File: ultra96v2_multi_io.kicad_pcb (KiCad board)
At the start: 2 copper layers, 85 x 54 mm, 85 parts, among them J1 TE 5179030-2, J2 57202-G52-20LF, J3 1-1734248-5, J4 1-1734248-5, J5 PMOD, J6 PMOD, J7 PinHeader, J8 Conn_01x04, Q1 DMN63D8LDW-7, Q2 DMN63D8LDW-7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

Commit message: rev2
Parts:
- J3, J4: footprint myfootprint:55510-140LF -> myfootprint:55510-140LF_handsolder
- L2: value 2.2uH MLZ2012A2R2MT -> 2.2uH 2012
- U1: value LM3671MF-3.3/NOPB -> LM3671MF-3.3
- moved R22 4.21 mm to (150.9, 129.7)
- moved C12 2.19 mm to (150.7, 134.5)
- moved C11 1.61 mm to (129.4, 133.0), turned to 180 degrees
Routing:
- net GND: track 554.3 -> 637.2 mm, vias 71 -> 88
- net /CAM1_SCL: track 41.7 -> 50.8 mm
- net /CAM1_CLK: track 44.0 -> 53.1 mm
- net /CAM1_SDA: track 44.3 -> 51.9 mm
- net /CAM1_GPIO: track 44.8 -> 52.4 mm, vias 1 -> 2
- net +3V3: track 172.9 -> 179.9 mm
- net /HS_CSI0_CLK_P: track 16.8 -> 10.3 mm
- net /HS_CSI0_D0_N: track 16.8 -> 22.3 mm
- net /CAM0_GPIO: track 17.0 -> 21.6 mm
- net /HS_SPI1_SCLK: track 14.5 -> 18.6 mm
- net /CAM0_CLK: track 14.6 -> 18.6 mm
- net /CAM0_SDA: track 18.5 -> 22.3 mm
- net /CAM0_SCL: track 17.5 -> 21.1 mm
- net /HS_CSI0_CLK_N: track 16.7 -> 13.1 mm
- net /HS_CSI1_D0_P: track 11.3 -> 14.4 mm
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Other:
- board text added: "96-MULTI-IO Rev.2 (C) Ryuji Fuchikami"
- board text removed: "96-MULTI-IO Rev.1 (C) Ryuji Fuchikami"

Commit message: update rev2
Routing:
- net GND: track 637.2 -> 631.5 mm, vias 88 -> 87
- net /HS_CSI1_D0_N: track 11.3 -> 14.0 mm
- net /HS_CSI1_D1_N: track 10.2 -> 12.5 mm
- net /HS_CSI1_D0_P: track 14.4 -> 16.5 mm
- net /HS_CSI1_D1_P: track 13.1 -> 15.3 mm
- net /HS_CSI1_CLK_N: track 12.4 -> 14.5 mm
- net /HS_CSI1_CLK_P: track 13.8 -> 15.6 mm

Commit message: update to rev3 add MIPI-SCI I2C pullup register
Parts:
- added R23: 4.7k, Resistor_SMD:R_0603_1608Metric, F.Cu at (116.6, 113.3)
- added R24: 4.7k, Resistor_SMD:R_0603_1608Metric, F.Cu at (118.2, 113.3)
- added R25: 4.7k, Resistor_SMD:R_0603_1608Metric, B.Cu at (149.2, 127.3)
- added R26: 4.7k, Resistor_SMD:R_0603_1608Metric, B.Cu at (153.8, 127.3)
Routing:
- net +3V3: track 179.9 -> 192.4 mm, vias 11 -> 12
- net /CAM0_SCL: track 21.1 -> 28.8 mm, vias 2 -> 3
- net /CAM0_SDA: track 22.3 -> 28.9 mm, vias 2 -> 3
- net /LS_I2C1_SDA: track 25.9 -> 28.4 mm
- net /CAM1_SCL: track 50.8 -> 53.1 mm
- net /CAM1_SDA: track 51.9 -> 53.8 mm
- net /CAM1_CLK: track 53.1 -> 53.7 mm
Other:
- board text added: "96-MULTI-IO Rev.3 (C) Ryuji Fuchikami"
- board text removed: "96-MULTI-IO Rev.2 (C) Ryuji Fuchikami"

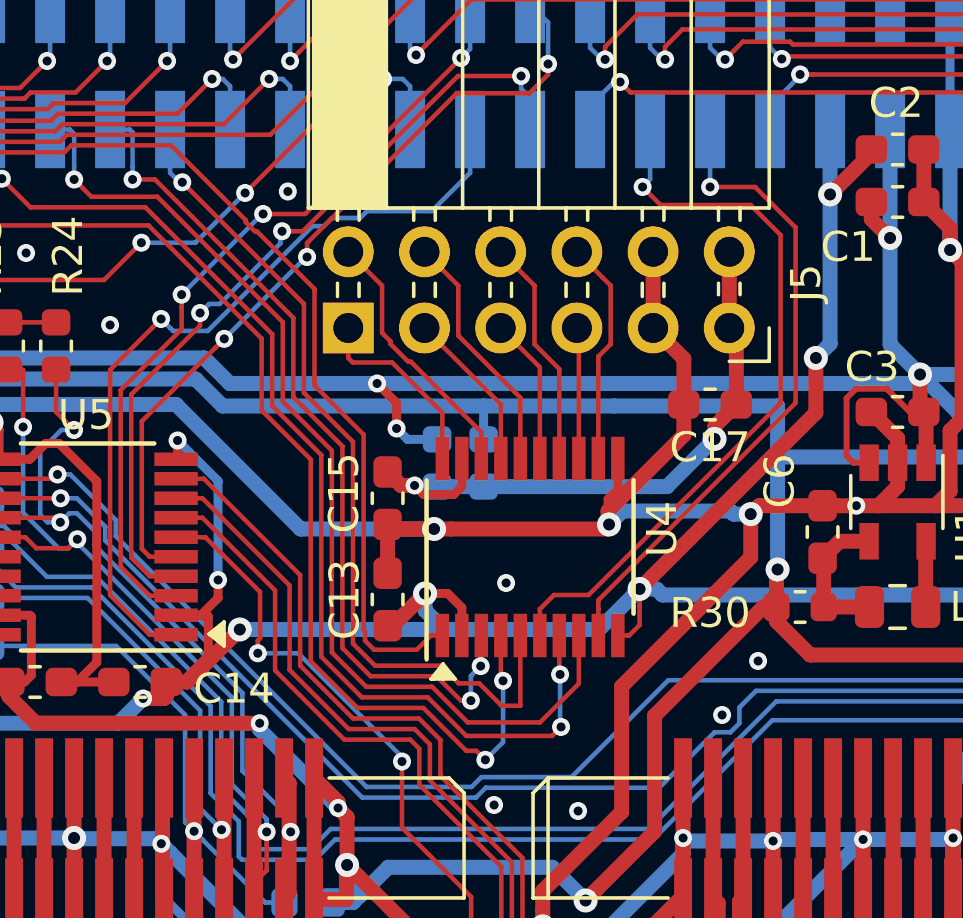
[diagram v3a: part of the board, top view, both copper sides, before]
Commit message: LS_GPIO_2 と LS_GPIO_6 の U4 への接続をスワップ
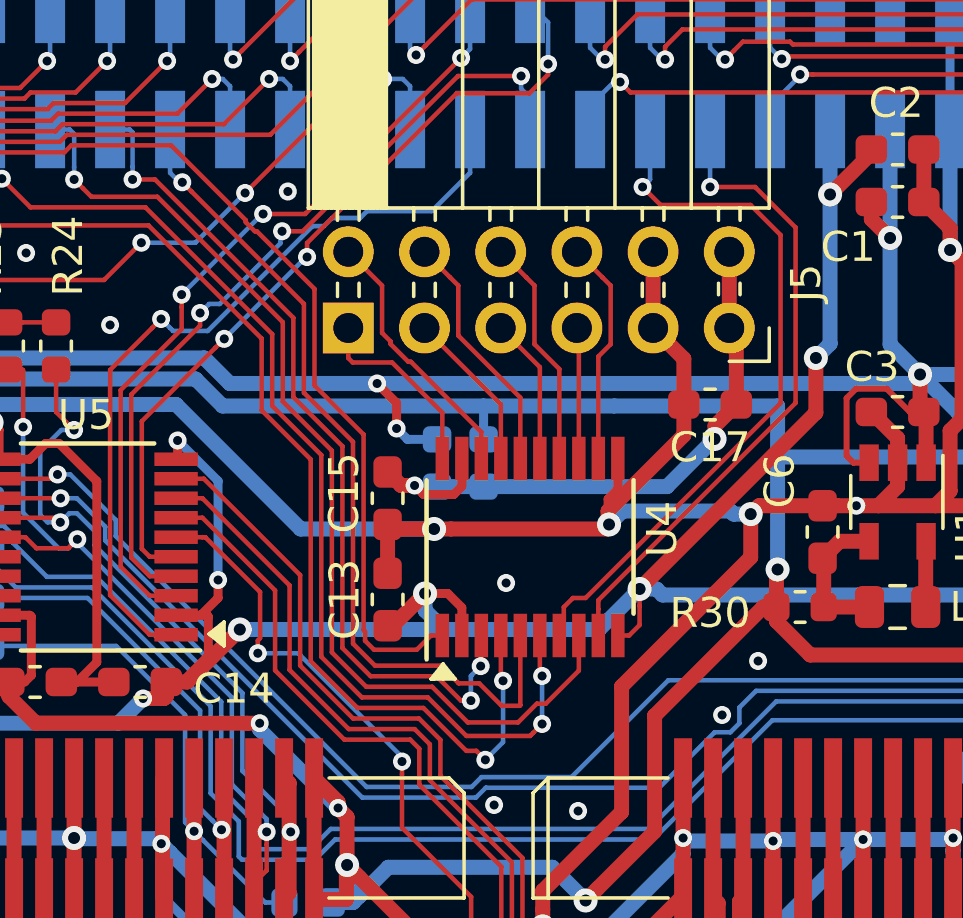
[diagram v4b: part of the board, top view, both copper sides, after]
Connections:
- U4 pad 6: /LS_GPIO_6 -> /LS_GPIO_2
- U4 pad 7: /LS_GPIO_2 -> /LS_GPIO_6
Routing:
- net /LS_GPIO_6: track 24.6 -> 23.9 mm
- net /LS_GPIO_2: track 36.8 -> 36.1 mm

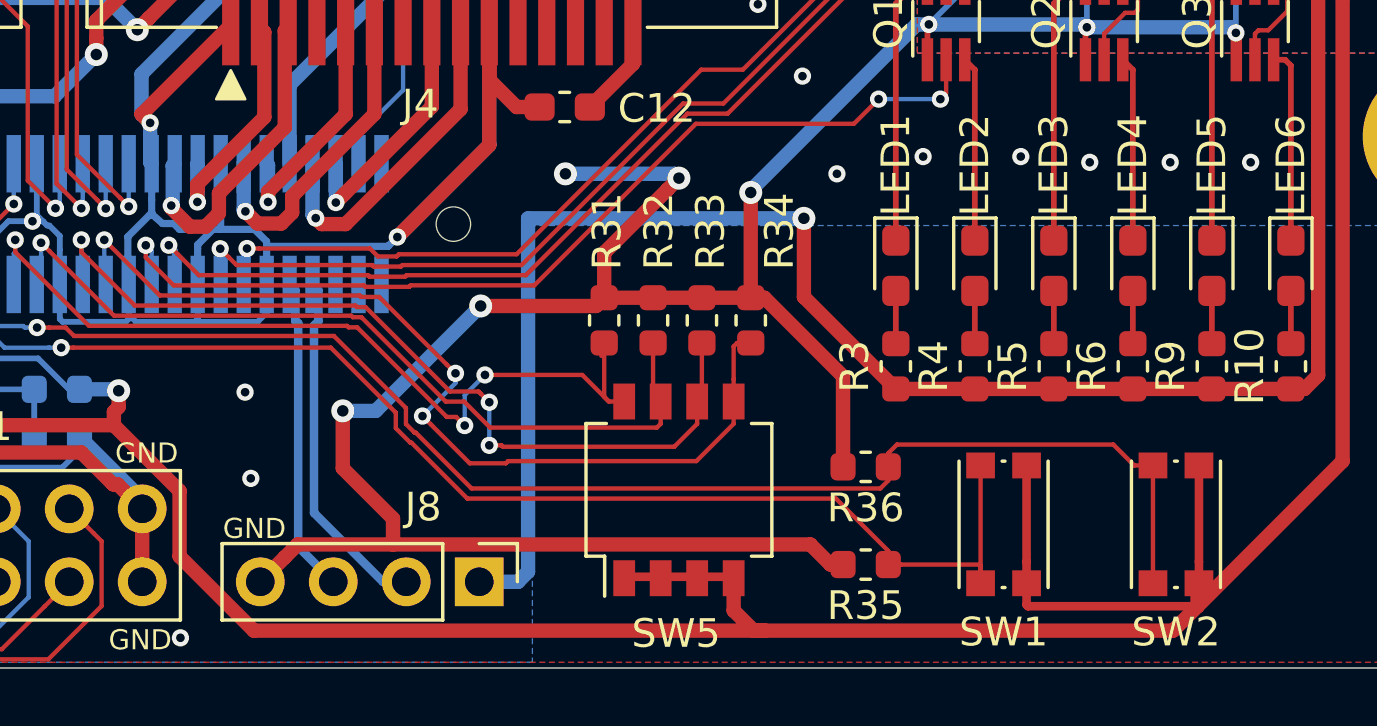
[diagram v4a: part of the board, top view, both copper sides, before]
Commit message: Q1-4 の DMN63D8LDW-7 -> DMN5L0-6DWK7 に変更(LVCMOS12対応) SW5 の GDH04S04 のフットプリントが A6H-4101 用になっていたので両対応パターンに変更
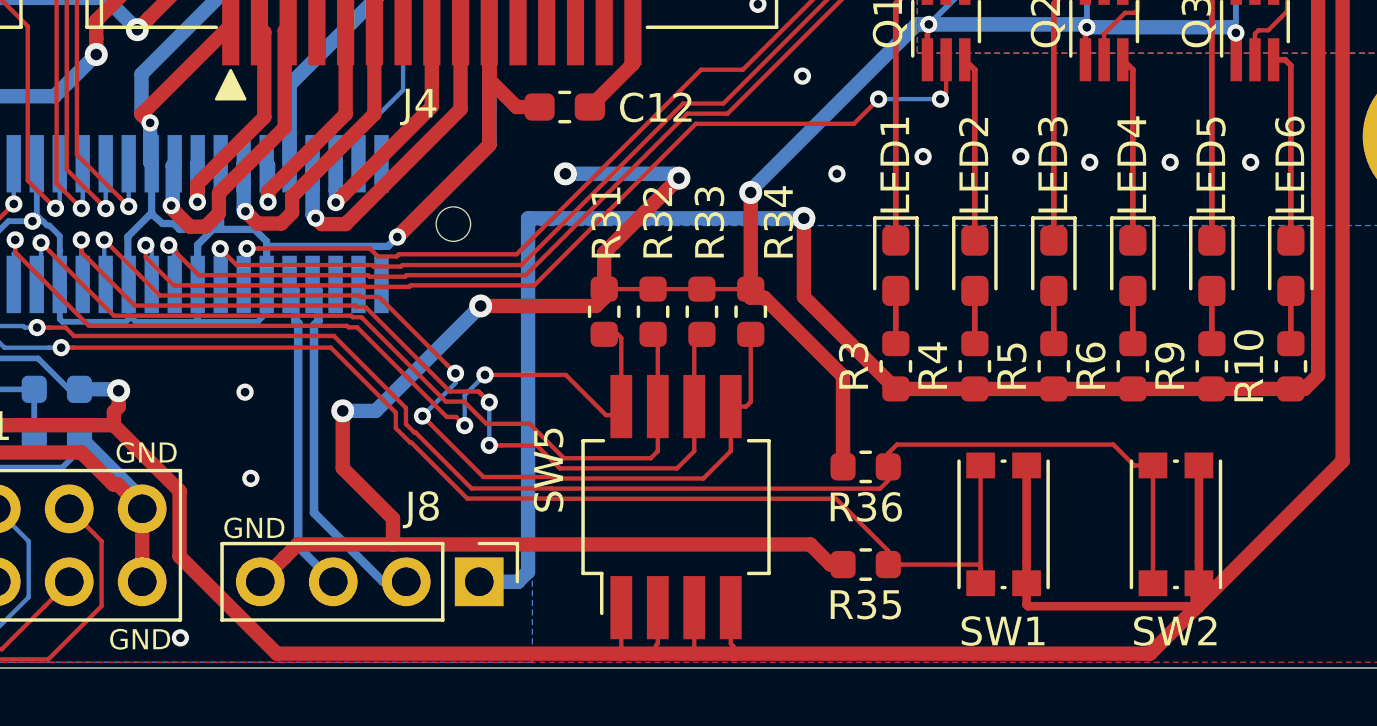
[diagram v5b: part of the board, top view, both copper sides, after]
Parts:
- Q1, Q2, Q3: value DMN63D8LDW-7 -> DMN5L0-6DWK7
- SW5: footprint Button_Switch_SMD:SW_DIP_SPSTx04_Slide_Omron_A6H-4101_W6.15mm_P1.27mm -> myfootprint:SW_DIP_multi_io
- moved SW5 0.61 mm to (154.6, 148.4)
- moved R31 0.30 mm to (152.1, 141.6)
- moved R32 0.30 mm to (153.8, 141.6)
- moved R33 0.30 mm to (155.5, 141.6)
- moved R34 0.30 mm to (157.2, 141.6)
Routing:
- net /HS_DSI_D1_P: track 30.3 -> 32.8 mm
- net /HS_DSI_D0_N: track 29.6 -> 30.7 mm
- net /HS_DSI_D1_N: track 33.1 -> 34.1 mm
- net +1V8: track 297.5 -> 298.3 mm
- net /HS_DSI_D0_P: track 30.0 -> 30.6 mm

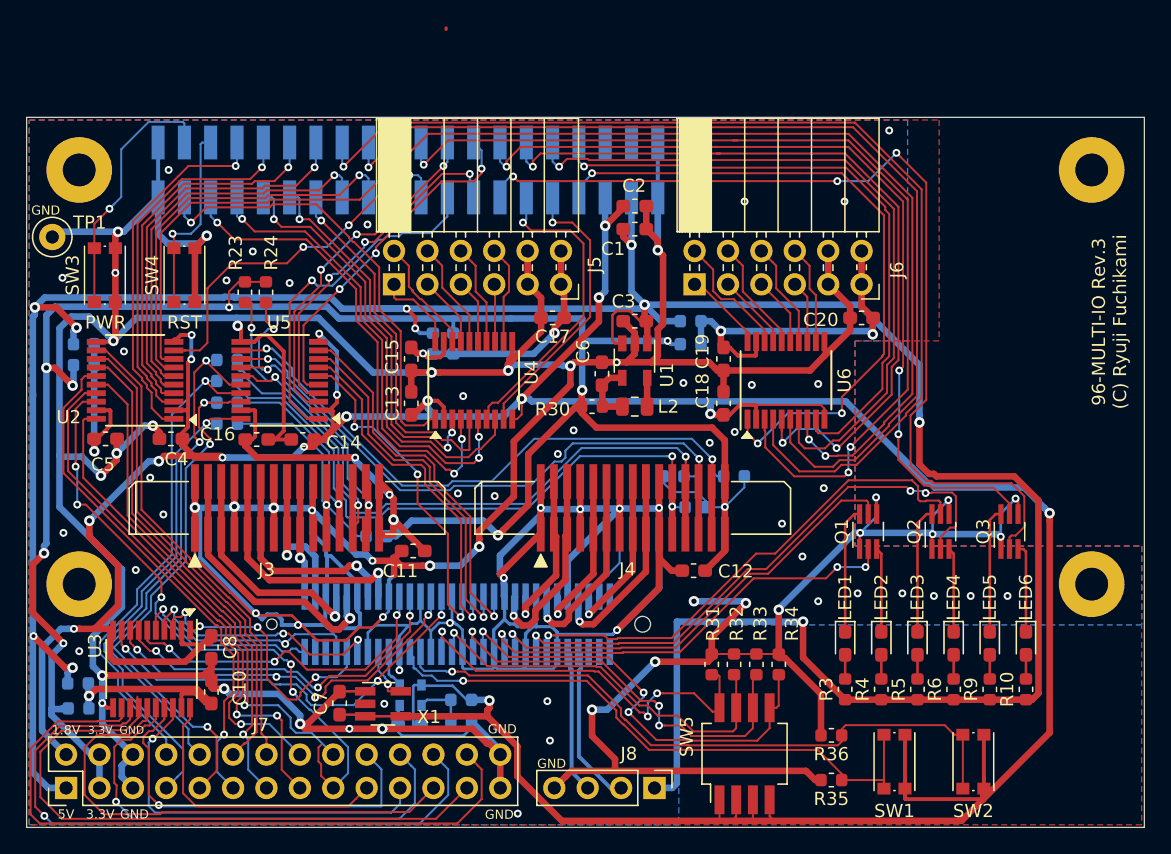
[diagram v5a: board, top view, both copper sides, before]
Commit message: HSコネクタの 1.2V信号を誤って 1.8V として扱っていた点を修正。
詳細はREADME参照の事
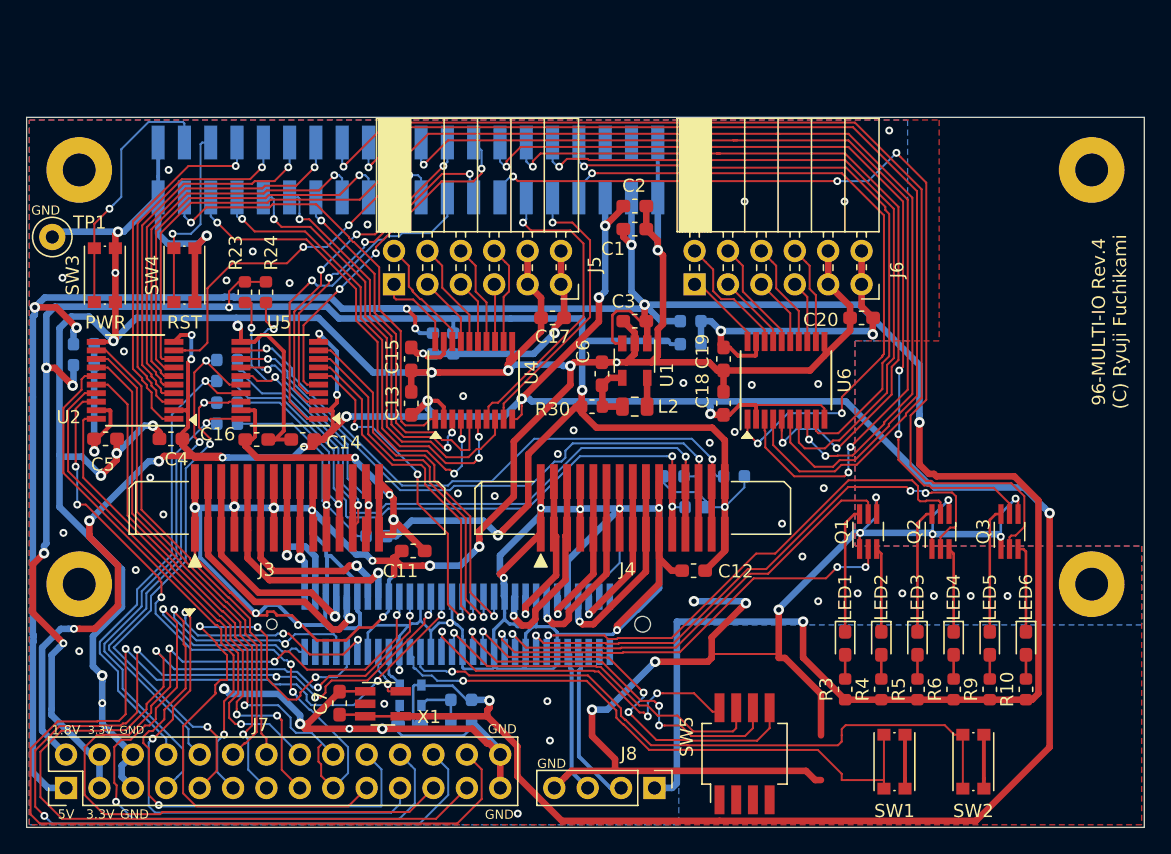
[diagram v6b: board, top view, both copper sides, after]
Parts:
- removed C10, C8: 0.1uF, Capacitor_SMD:C_0603_1608Metric_Pad1.05x0.95mm_HandSolder
- removed R11: 0, Resistor_SMD:R_0603_1608Metric
- removed R12: <0>, Resistor_SMD:R_0603_1608Metric
- removed R31, R32, R33, R34, R35, R36: 4.7k, Resistor_SMD:R_0603_1608Metric
- removed U3: TXS0108EPW, Package_SO:TSSOP-20_4.4x6.5mm_P0.65mm
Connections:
- J1 pad 3: Net-(J1-Pad3) -> unconnected-(J1-Pin_3-Pad3)
- J1 pad 5: Net-(J1-Pad5) -> unconnected-(J1-Pin_5-Pad5)
- J1 pad 57: Net-(J1-Pad57) -> unconnected-(J1-Pin_57-Pad57)
- J1 pad 59: Net-(J1-Pad59) -> unconnected-(J1-Pin_59-Pad59)
- J1 pad 60: Net-(J1-Pad60) -> unconnected-(J1-Pin_60-Pad60)
- J7 pad 19: /PH_SPI1_SCLK -> /HS_SPI1_SCLK
- J7 pad 20: /PH_SPI1_CS -> /HS_SPI1_CS
- J7 pad 21: /PH_SPI1_MISO -> /HS_SPI1_MISO
- J7 pad 22: /PH_SPI1_MOSI -> /HS_SPI1_MOSI
- J7 pad 23: /PH_GPIO_A -> /HS_CSI0_D2_P
- J7 pad 24: /PH_GPIO_C -> /HS_CSI0_D3_P
- J7 pad 25: /PH_GPIO_B -> /HS_CSI0_D2_N
- J7 pad 26: /PH_GPIO_D -> /HS_CSI0_D3_N
- SW1 pad 2: +1V8 -> GND
- SW2 pad 2: +1V8 -> GND
- SW5 pad 1: +1V8 -> GND
- SW5 pad 2: +1V8 -> GND
- SW5 pad 3: +1V8 -> GND
- SW5 pad 4: +1V8 -> GND
- X1 pad 2: Net-(X1-Pad2) -> unconnected-(X1-NC-Pad2)
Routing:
- net /HS_CSI0_D3_N: track 31.9 -> 87.9 mm
- net /PH_GPIO_D: track 52.9 -> 0.00 mm
- net /HS_CSI0_D3_P: track 30.0 -> 82.6 mm, vias 4 -> 5
- net /HS_CSI0_D2_N: track 27.3 -> 77.0 mm
- net /PH_GPIO_C: track 49.7 -> 0.00 mm, vias 1 -> 0
- net /PH_GPIO_B: track 47.6 -> 0.00 mm
- net /HS_SPI1_MOSI: track 14.4 -> 58.2 mm, vias 1 -> 2
- net /HS_CSI0_D2_P: track 25.6 -> 66.1 mm
- net +1V8: track 298.3 -> 259.9 mm
- net /PH_GPIO_A: track 38.1 -> 0.00 mm
- net /PH_SPI1_MOSI: track 37.1 -> 0.00 mm, vias 1 -> 0
- net /HS_SPI1_CS: track 17.2 -> 53.9 mm, vias 2 -> 3
- net /HS_SPI1_MISO: track 18.4 -> 53.5 mm, vias 3 -> 4
- net /PH_SPI1_CS: track 30.3 -> 0.00 mm, vias 1 -> 0
- net /HS_SPI1_SCLK: track 18.6 -> 47.9 mm
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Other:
- net class Default removed
- board text added: "96-MULTI-IO Rev.4 (C) Ryuji Fuchikami"
- board text removed: "96-MULTI-IO Rev.3 (C) Ryuji Fuchikami"

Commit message: 未接続ネットの削除など
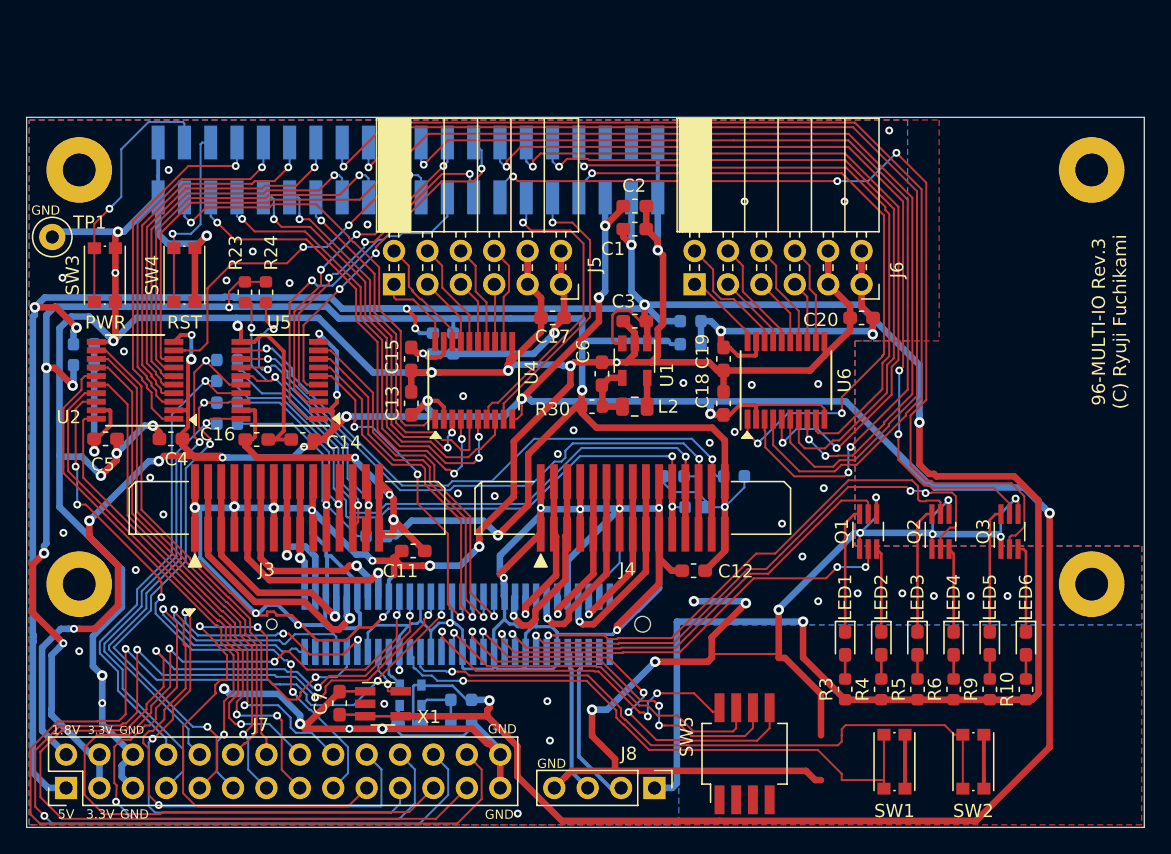
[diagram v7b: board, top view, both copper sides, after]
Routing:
- net /PH_SPI0_MISO: track 48.1 -> 44.3 mm
- net /LS_GPIO_13: track 60.7 -> 59.6 mm
- net /LS_GPIO_0: track 35.0 -> 34.4 mm
- net /HS_CSI1_MCLK: track 3.50 -> 2.93 mm
- net /HS_SPI1_CS: vias 3 -> 2
- net /HS_CSI0_D3_P: vias 5 -> 4
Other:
- board text added: "96-MULTI-IO Rev.3 (C) Ryuji Fuchikami"
- board text removed: "96-MULTI-IO Rev.4 (C) Ryuji Fuchikami"
